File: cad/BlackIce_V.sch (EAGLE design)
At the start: 62 parts, among them IC1 REG1117, IC2 STM32F103C6T7A, IC3 ICE40UP5K, IC4 SPX3819M5_1_2, IC5 AT25SDF041A, IC6 AT25SDF041A, X1 HC49UP

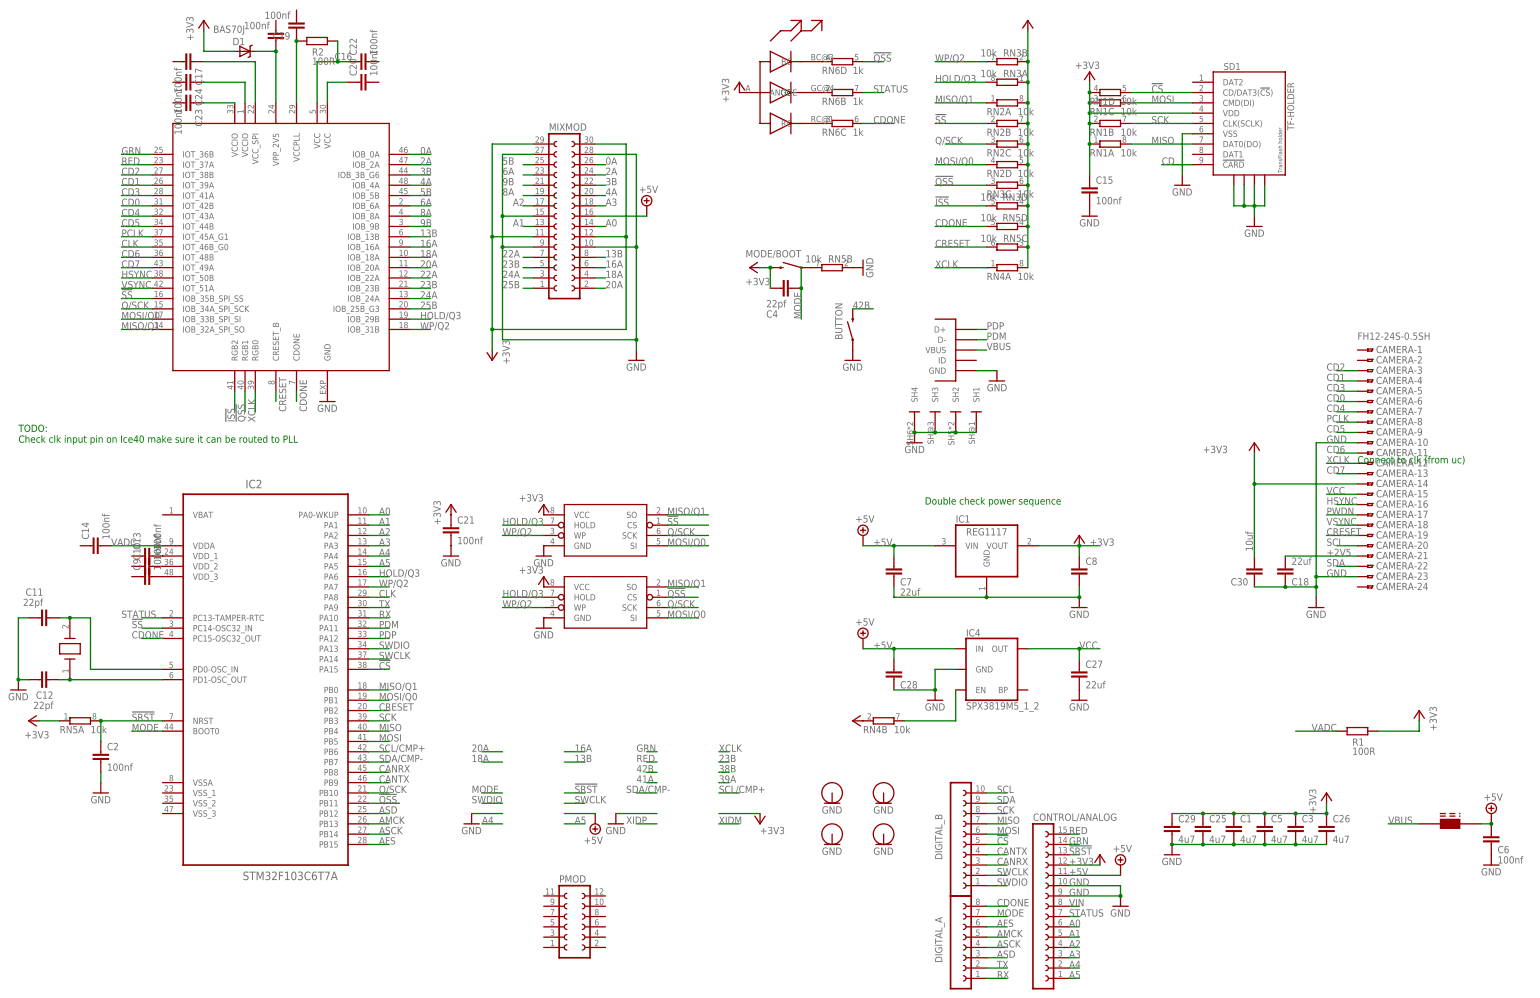
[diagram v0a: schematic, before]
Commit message: Cleaned up the schematic a little and soretyed the Pmod signals (shared with Cam data)
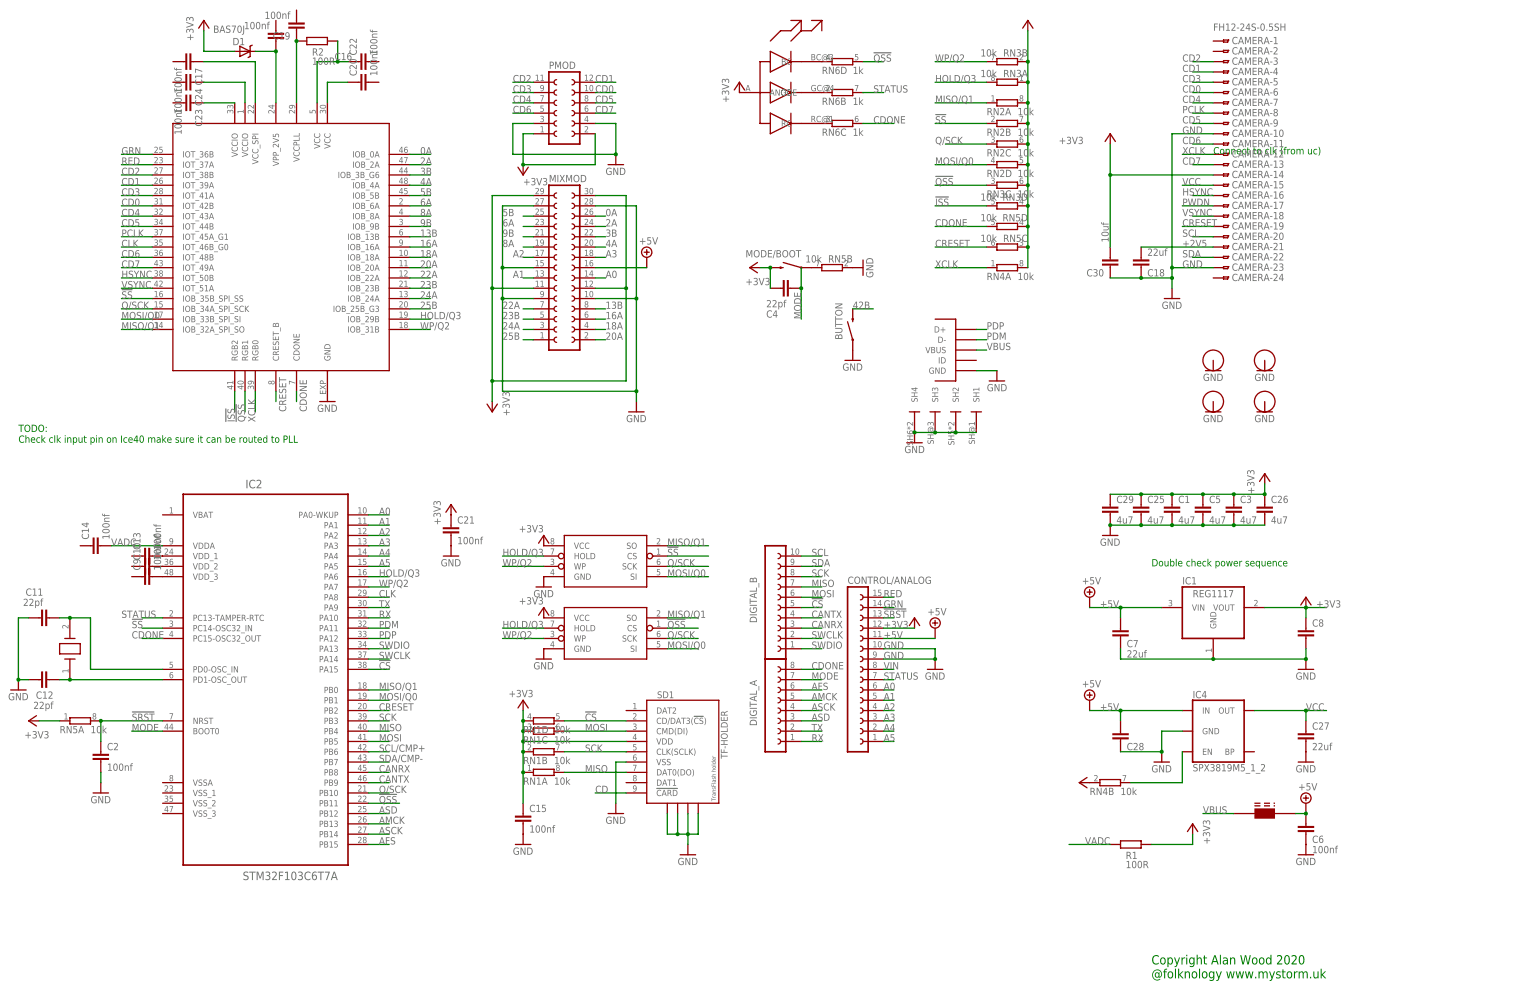
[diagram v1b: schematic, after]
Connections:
- net +3V3: now also PMOD.1, PMOD.2
- net CD0: now also PMOD.10
- net CD1: now also PMOD.12
- net CD2: now also PMOD.11
- net CD3: now also PMOD.9
- net CD4: now also PMOD.7
- net CD5: now also PMOD.8
- net CD6: now also PMOD.5
- net CD7: now also PMOD.6
- net GND: now also PMOD.3, PMOD.4
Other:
- note added: "Copyright Alan Wood 2020 @folknology www.mystorm.uk"
- moved on the sheet: C1, C15, C18, C25, C26, C27, C28, C29, C3, C30, C5, C6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
